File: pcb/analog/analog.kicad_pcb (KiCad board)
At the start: 2 copper layers, 70 x 70 mm, 65 parts, among them J1 USB_C_Receptacle_USB2.0, SW1 SW_Push, SW2 SW_Push, U1 SRV05-4, U2 XC6206P332MR, U3 DRV5056A3xDBZxQ1, U4 DRV5056A3xDBZxQ1, U5 DRV5056A3xDBZxQ1, U6 74AHCT1G125, U7 74AHCT1G125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

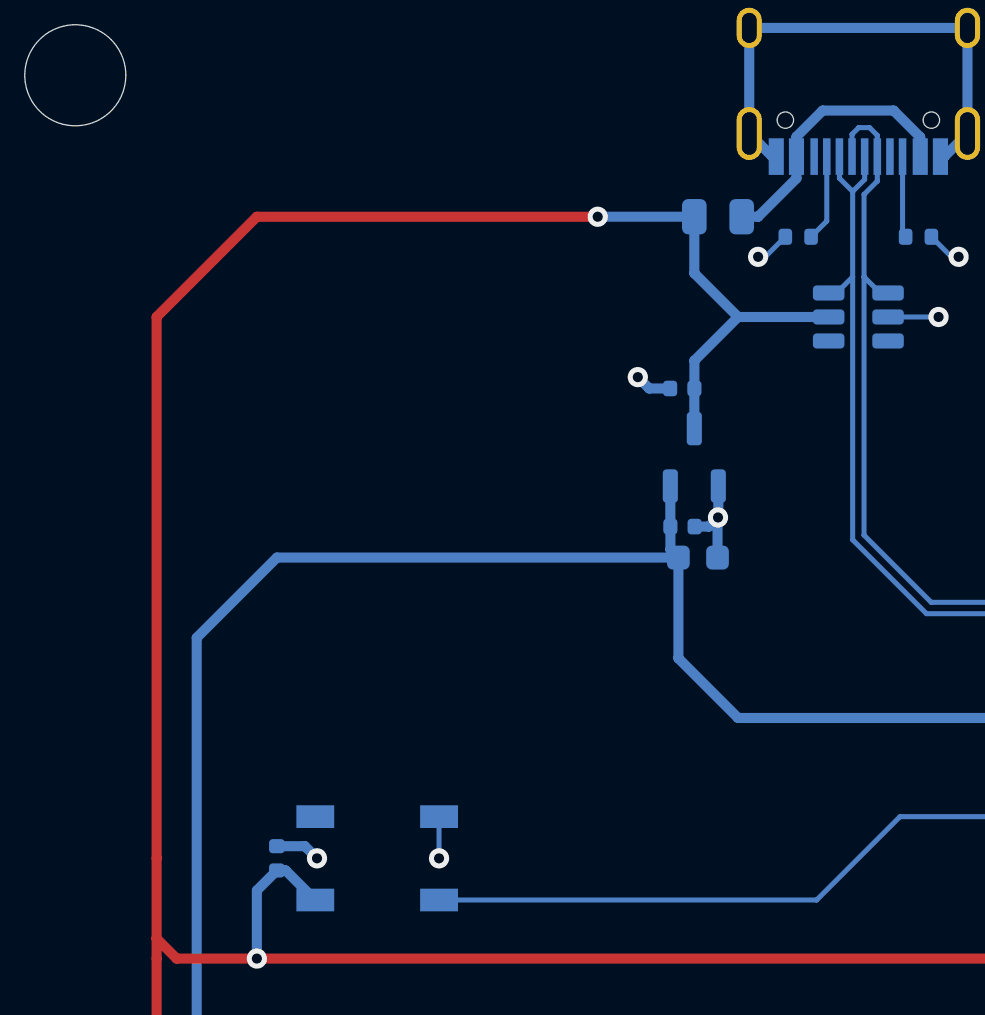
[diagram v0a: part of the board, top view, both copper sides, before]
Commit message: refactor: use 1206 footprint for fuse
there are more polyfuses with 500mA hold current at this size.
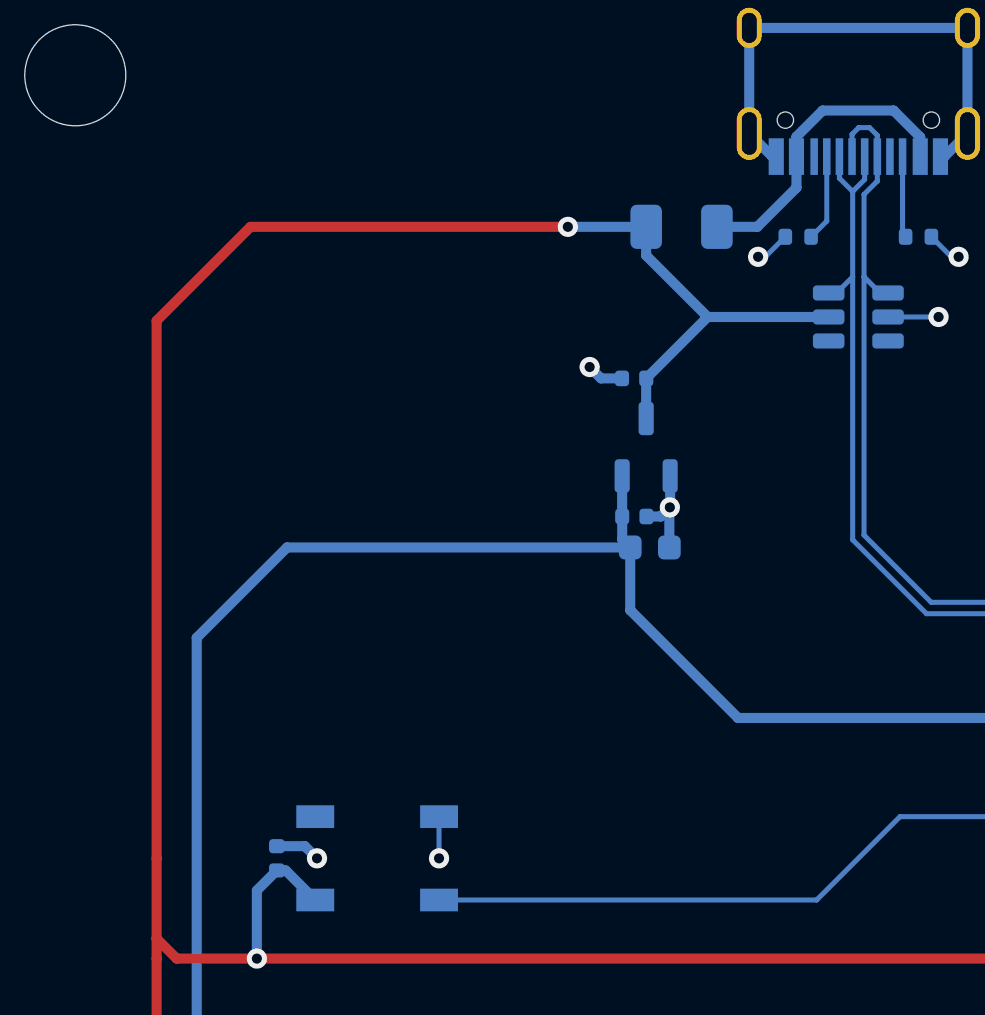
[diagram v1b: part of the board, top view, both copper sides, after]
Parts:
- F1: footprint Fuse:Fuse_0805_2012Metric -> Fuse:Fuse_1206_3216Metric
- moved C4 1.95 mm to (41.9, 31.8)
- moved C15 1.95 mm to (42.5, 38.5)
- moved C5 1.95 mm to (41.9, 37.3)
- moved U2 1.95 mm to (42.4, 34.5)
- moved F1 1.50 mm to (43.8, 25.8)
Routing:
- net VBUS: track 11.0 -> 12.3 mm
- net +5V: track 214.2 -> 213.0 mm
- net +3V3: track 212.2 -> 211.7 mm

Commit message: feat: setup jlcpcb tools
seems to be working - the generated gerbers, bom and cpl are correct.

the DRV5056 isn't being picked up, but it's likely just because it's out of stock.
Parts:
- U9: value W25Q128JVS -> W25Q16JVSSIQ

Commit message: feat: add jlc order number placeholder
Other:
- board text added: "JLCJLCJLCJLC"
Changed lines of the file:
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@@
   (gr_arc (start 83.8 15.8) (mid 85.214209 16.385791) (end 85.8 17.8)
     (stroke (width 0.1) (type default)) (layer "Edge.Cuts"))
+  (gr_text "JLCJLCJLCJLC" (at 79.3 84.8) (layer "B.SilkS")
+    (effects (font (size 0.8 0.8) (thickness 0.15)) (justify left bottom mirror))
+  )
   (gr_text "SEL" (at 68.8 24.604913) (layer "B.SilkS")
     (effects (font (size 1 0.8) (thickness 0.15)) (justify mirror))

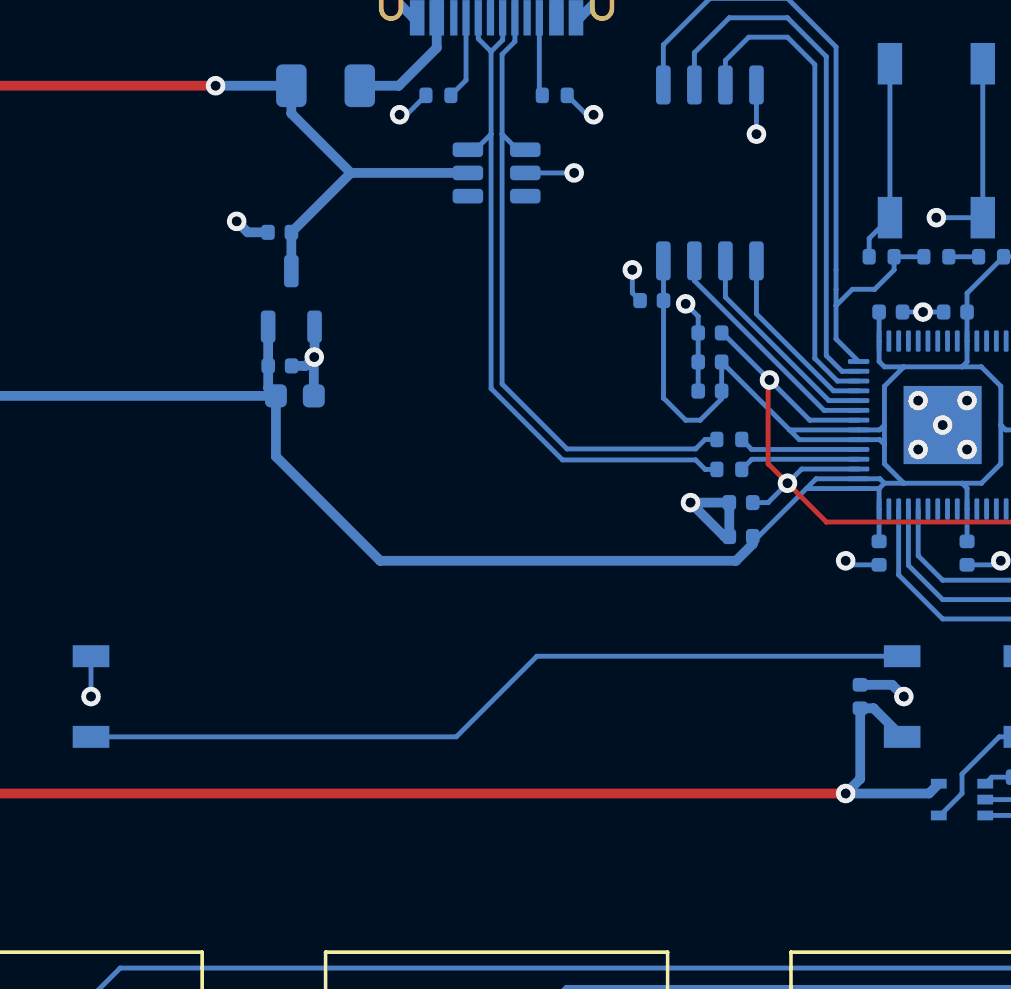
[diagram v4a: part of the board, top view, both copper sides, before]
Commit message: feat: add haruka-16 to pcb again
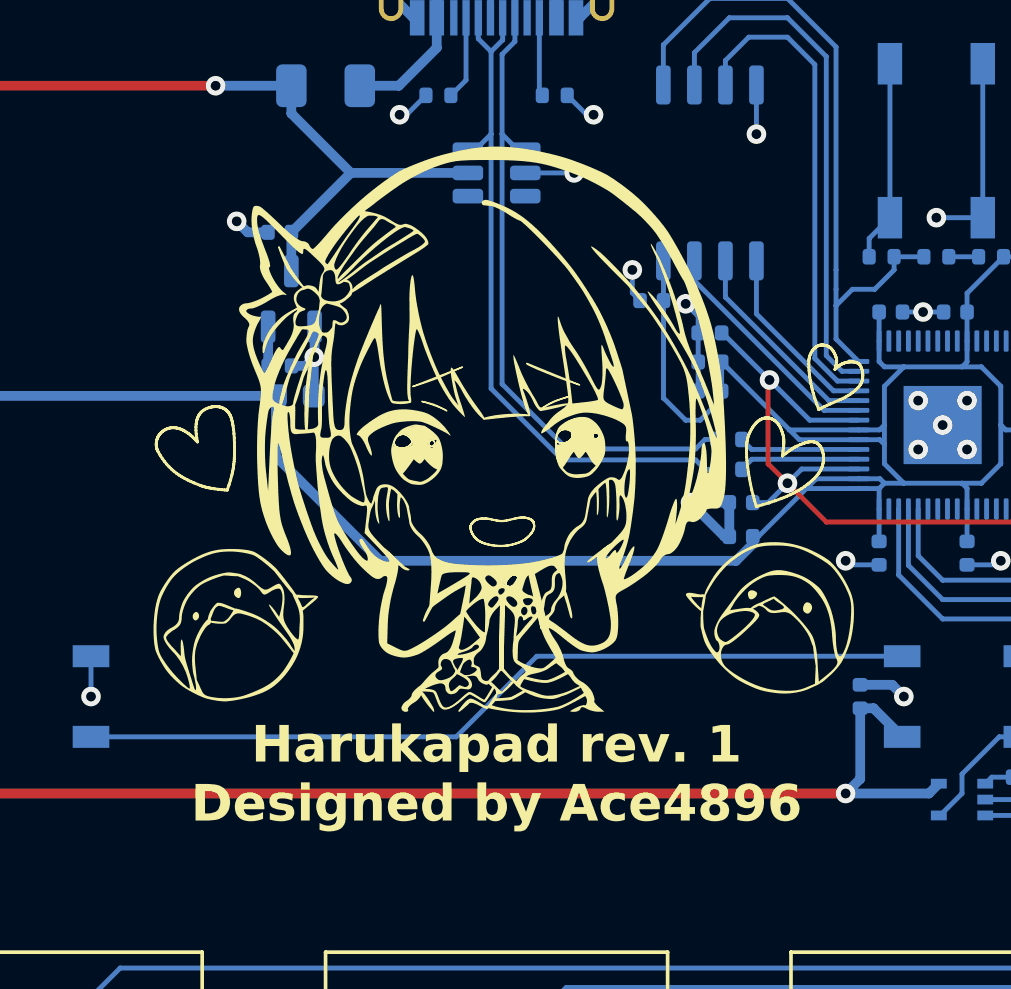
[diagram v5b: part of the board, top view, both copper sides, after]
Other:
- board text added: "Harukapad rev. 1 Designed by Ace4896"
